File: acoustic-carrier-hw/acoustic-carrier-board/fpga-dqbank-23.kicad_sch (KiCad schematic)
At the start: 13 parts, among them IC1 ECP5-BGA256

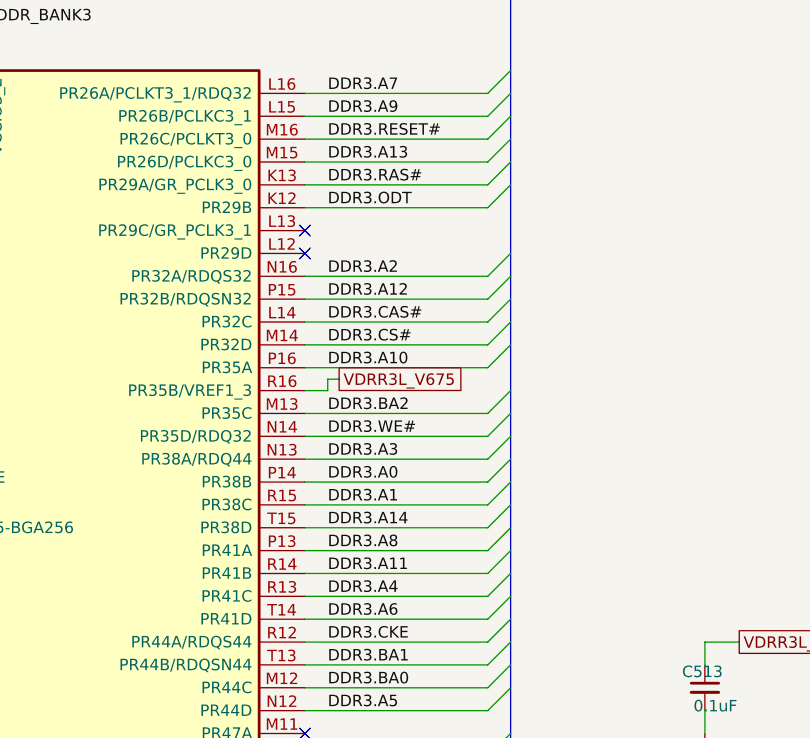
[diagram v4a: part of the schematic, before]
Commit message: [carrier] Progressing on ddr3 routing (next) check all ddr3 signals for errors, start length matching
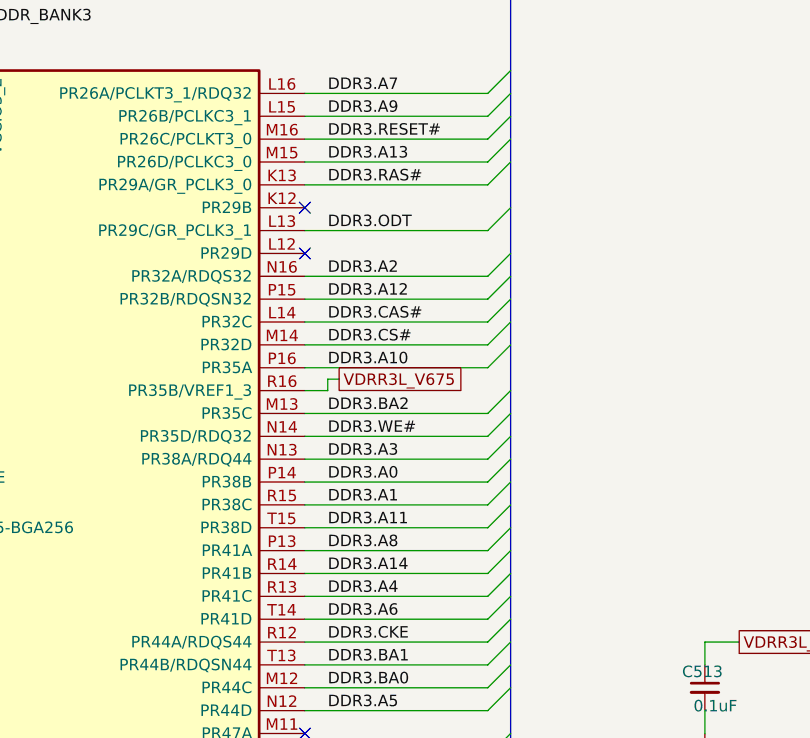
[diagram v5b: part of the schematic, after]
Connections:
- net DDR3.A11: now also IC1.T15 (PR38D); no longer IC1.R14 (PR41B)
- net DDR3.A14: now also IC1.R14 (PR41B); no longer IC1.T15 (PR38D)
- net DDR3.ODT: now also IC1.L13 (PR29C/GR_PCLK3_1); no longer IC1.K12 (PR29B)
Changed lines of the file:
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@@
+	)
+	(no_connect
+		(at 212.09 71.12)
 	)
 	(no_connect
@@
 		(at 71.12 92.71)
 	)
-	(no_connect
-		(at 212.09 73.66)
-	)
 	(bus_entry
 		(at 234.95 81.28)
@@
 	)
 	(bus_entry
+		(at 234.95 71.12)
+		(size -2.54 2.54)
+		(stroke
+			(width 0)
+			(type default)
+		)
+	)
+	(bus_entry
 		(at 234.95 63.5)
 		(size -2.54 2.54)
@@
 	)
 	(bus_entry
-		(at 234.95 68.58)
-		(size -2.54 2.54)
-		(stroke
-			(width 0)
-			(type default)
-		)
-	)
-	(bus_entry
 		(at 234.95 83.82)
 		(size -2.54 2.54)
@@
 	(bus
 		(pts
+			(xy 234.95 71.12) (xy 234.95 76.2)
+		)
+		(stroke
+			(width 0)
+			(type default)
+		)
+	)
+	(bus
+		(pts
 			(xy 104.14 125.73) (xy 104.14 113.03)
 		)
@@
 	(bus
 		(pts
-			(xy 234.95 66.04) (xy 234.95 68.58)
+			(xy 234.95 66.04) (xy 234.95 71.12)
 		)
 		(stroke
@@
 		)
 	)
-	(wire
-		(pts
-			(xy 212.09 71.12) (xy 232.41 71.12)
-		)
-		(stroke
-			(width 0)
-			(type default)
-		)
-	)
 	(bus
 		(pts
@@
 		)
 	)
-	(bus
-		(pts
-			(xy 234.95 68.58) (xy 234.95 76.2)
-		)
-		(stroke
-			(width 0)
-			(type default)
-		)
-	)
 	(wire
 		(pts
@@
 		(pts
 			(xy 71.12 125.73) (xy 101.6 125.73)
+		)
+		(stroke
+			(width 0)
+			(type default)
+		)
+	)
+	(wire
+		(pts
+			(xy 212.09 73.66) (xy 232.41 73.66)
 		)
 		(stroke
@@
 		)
 	)
+	(label "DDR3.A11"
+		(at 214.63 106.68 0)
+		(effects
+			(font
+				(size 1.27 1.27)
+			)
+			(justify left bottom)
+		)
+	)
 	(label "DDR3.A5"
 		(at 214.63 127 0)
@@
 		)
 	)
-	(label "DDR3.A11"
-		(at 214.63 111.76 0)
-		(effects
-			(font
-				(size 1.27 1.27)
-			)
-			(justify left bottom)
-		)
-	)
 	(label "DDR3.DQ9"
 		(at 88.9 69.85 180)
@@
 		)
 	)
-	(label "DDR3.A14"
-		(at 214.63 106.68 0)
-		(effects
-			(font
-				(size 1.27 1.27)
-			)
-			(justify left bottom)
-		)
-	)
 	(label "DDR3.CS#"
 		(at 214.63 86.36 0)
@@
 		)
 	)
+	(label "DDR3.A14"
+		(at 214.63 111.76 0)
+		(effects
+			(font
+				(size 1.27 1.27)
+			)
+			(justify left bottom)
+		)
+	)
 	(label "DDR3.CAS#"
 		(at 214.63 83.82 0)
@@
 		)
 	)
+	(label "DDR3.ODT"
+		(at 214.63 73.66 0)
+		(effects
+			(font
+				(size 1.27 1.27)
+			)
+			(justify left bottom)
+		)
+	)
 	(label "DDR3.DQ6"
 		(at 87.63 110.49 0)
 		(effects
 			(font
-				(size 1.27 1.27)
-			)
-			(justify left bottom)
-		)
-	)
-	(label "DDR3.ODT"
-		(at 214.63 71.12 0)
-		(effects
-			(font

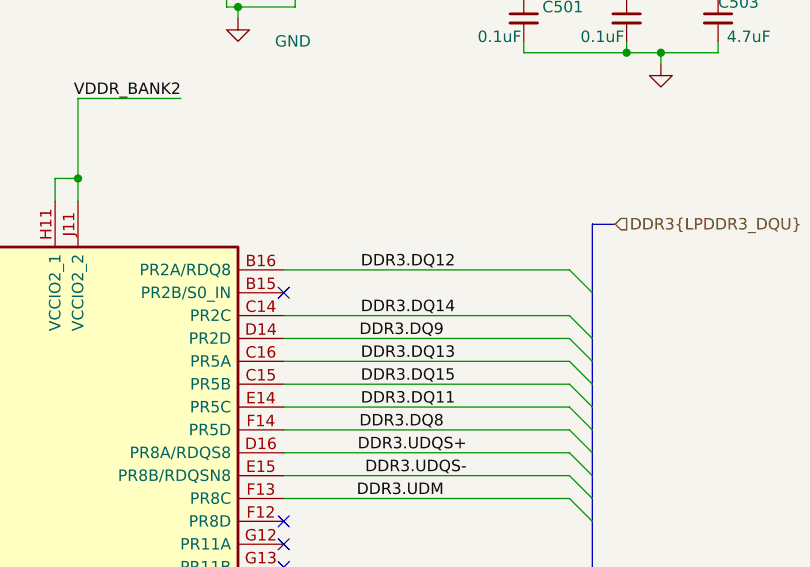
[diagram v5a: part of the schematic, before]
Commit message: [carrier] Changed all vias to (pcheaper) 0.2/0.35 size (next) create basic test-VHDL for clock-signal fanout checks
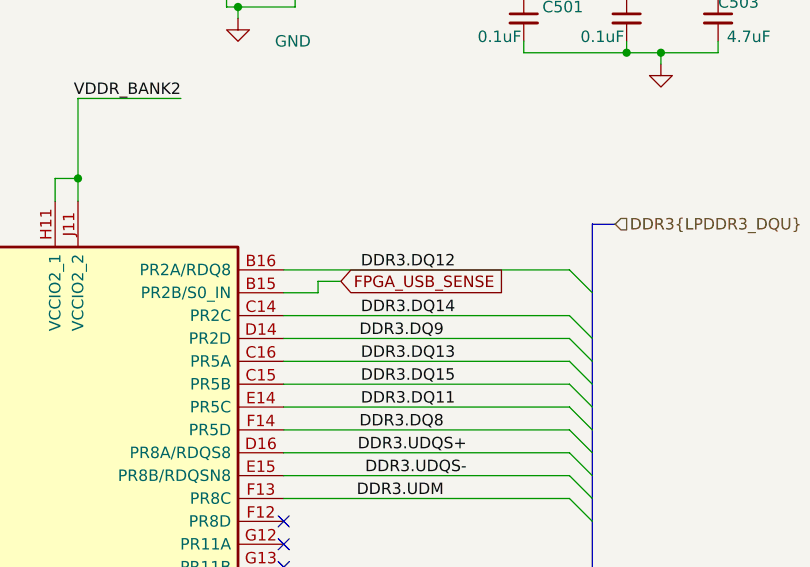
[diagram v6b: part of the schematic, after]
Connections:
- net FPGA_USB_SENSE: now reaches IC1.B15 (PR2B/S0_IN)
- no-connect marks 13 -> 12
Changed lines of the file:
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@@
-	)
-	(no_connect
-		(at 71.12 64.77)
 	)
 	(no_connect
@@
 	(wire
 		(pts
+			(xy 74.93 63.5) (xy 74.93 64.77)
+		)
+		(stroke
+			(width 0)
+			(type default)
+		)
+	)
+	(wire
+		(pts
 			(xy 245.11 36.83) (xy 245.11 38.1)
 		)
@@
 		)
 	)
+	(wire
+		(pts
+			(xy 74.93 64.77) (xy 71.12 64.77)
+		)
+		(stroke
+			(width 0)
+			(type default)
+		)
+	)
 	(bus
 		(pts
@@
 		(pts
 			(xy 71.12 138.43) (xy 101.6 138.43)
+		)
+		(stroke
+			(width 0)
+			(type default)
+		)
+	)
+	(wire
+		(pts
+			(xy 74.93 63.5) (xy 77.47 63.5)
 		)
 		(stroke
@@
 			(effects
 				(font
+					(size 1.27 1.27)
+				)
+				(justify left)
+				(hide yes)
+			)
+		)
+	)
+	(global_label "FPGA_USB_SENSE"
+		(shape input)
+		(at 77.47 63.5 0)
+		(fields_autoplaced yes)
+		(effects
+			(font
+				(size 1.27 1.27)
+			)
+			(justify left)
+		)
+		(property "Intersheetrefs" "${INTERSHEET_REFS}"
+			(at 96.9651 63.5 0)
+			(effects
+				(font

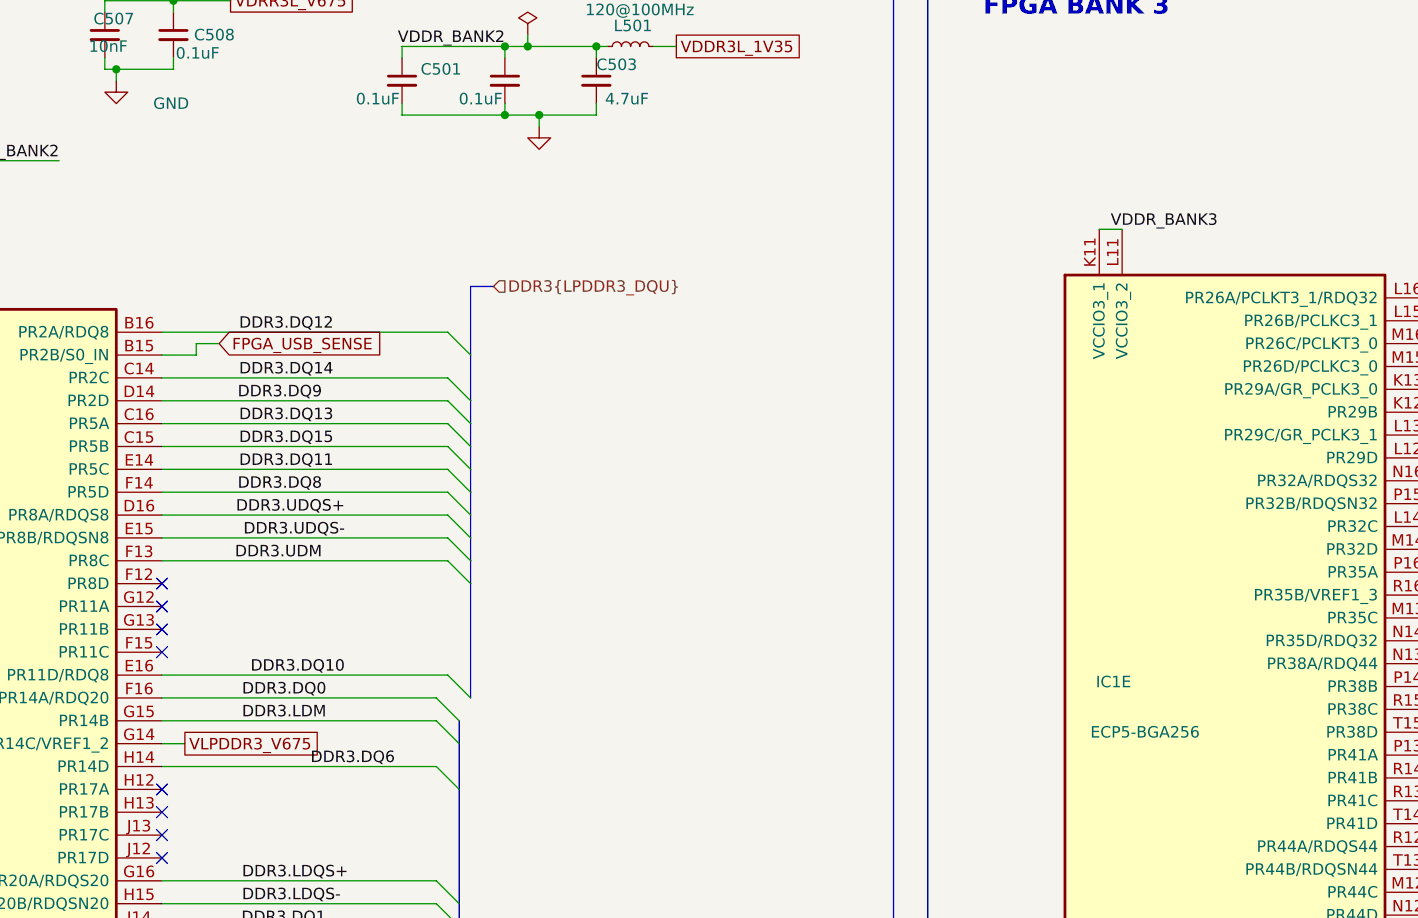
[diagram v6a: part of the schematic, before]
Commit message: [carrier] Started writing constraints file for ECP5U-FPGA (next) finish constraints file, try basic synthesis with pins and hello-world
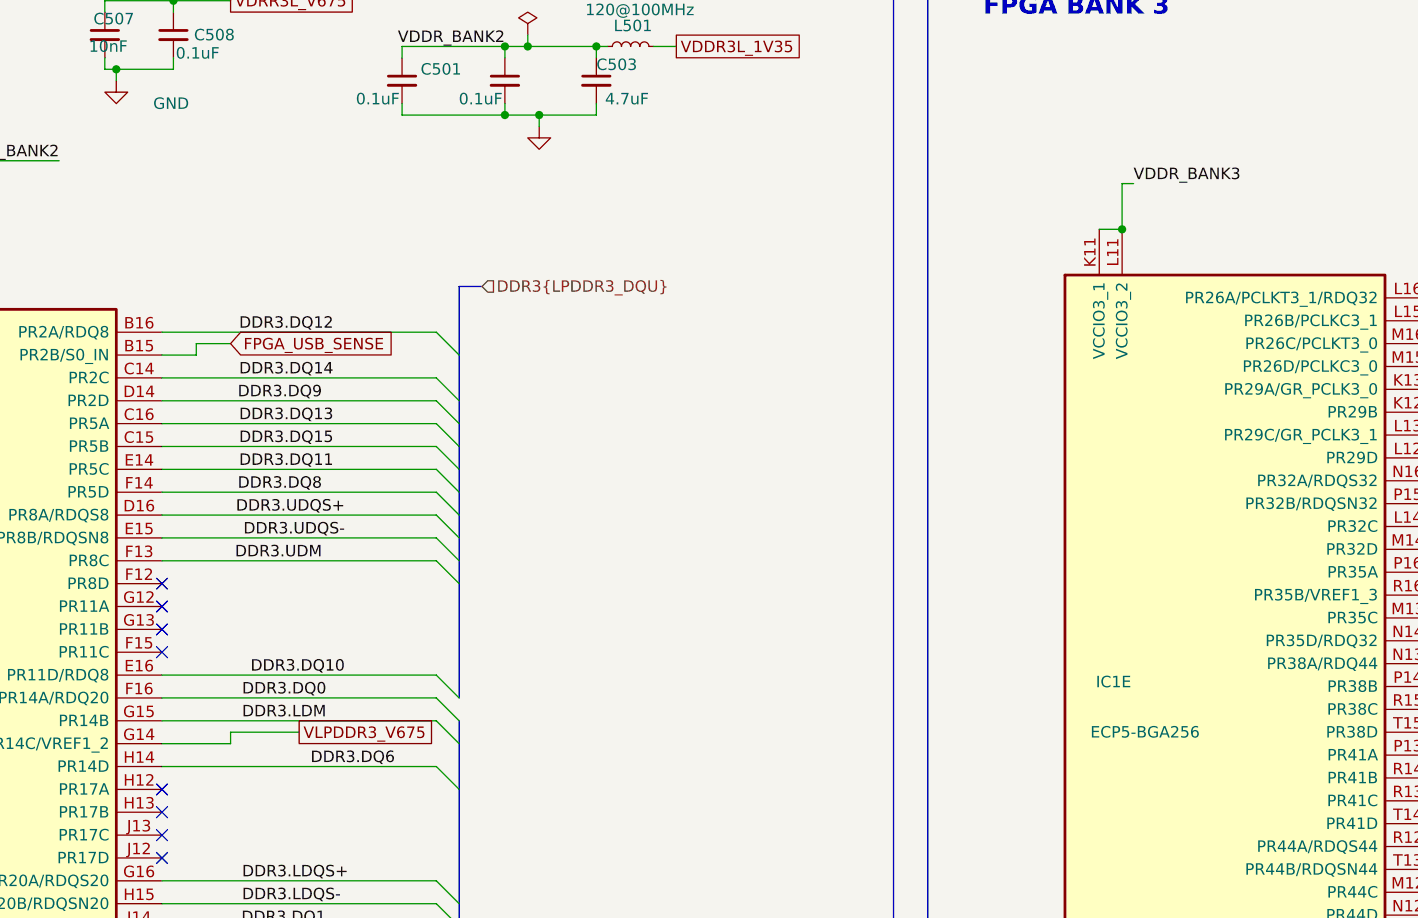
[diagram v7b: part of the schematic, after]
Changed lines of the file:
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@@
+	)
+	(junction
+		(at 177.8 50.8)
+		(diameter 0)
+		(color 0 0 0 0)
 	)
 	(junction
@@
 	)
 	(bus_entry
-		(at 105.41 90.17)
+		(at 104.14 90.17)
 		(size -2.54 -2.54)
 		(stroke
@@
 	)
 	(bus_entry
-		(at 102.87 72.39)
+		(at 101.6 72.39)
 		(size 2.54 2.54)
 		(stroke
@@
 	)
 	(bus_entry
-		(at 105.41 64.77)
+		(at 104.14 64.77)
 		(size -2.54 -2.54)
 		(stroke
@@
 	)
 	(bus_entry
-		(at 105.41 85.09)
+		(at 104.14 85.09)
 		(size -2.54 -2.54)
 		(stroke
@@
 	)
 	(bus_entry
-		(at 105.41 80.01)
+		(at 104.14 80.01)
 		(size -2.54 -2.54)
 		(stroke
@@
 	)
 	(bus_entry
-		(at 105.41 87.63)
+		(at 104.14 87.63)
 		(size -2.54 -2.54)
 		(stroke
@@
 	)
 	(bus_entry
-		(at 105.41 72.39)
+		(at 104.14 72.39)
 		(size -2.54 -2.54)
 		(stroke
@@
 	)
 	(bus_entry
-		(at 105.41 82.55)
+		(at 104.14 82.55)
 		(size -2.54 -2.54)
 		(stroke
@@
 	)
 	(bus_entry
-		(at 105.41 69.85)
+		(at 104.14 69.85)
 		(size -2.54 -2.54)
 		(stroke
@@
 	)
 	(bus_entry
-		(at 102.87 100.33)
+		(at 101.6 100.33)
 		(size 2.54 2.54)
 		(stroke
@@
 	)
 	(bus_entry
-		(at 105.41 77.47)
+		(at 104.14 77.47)
 		(size -2.54 -2.54)
 		(stroke
@@
 	(bus
 		(pts
-			(xy 105.41 85.09) (xy 105.41 82.55)
-		)
-		(stroke
-			(width 0)
-			(type default)
-		)
-	)
-	(wire
-		(pts
-			(xy 71.12 69.85) (xy 102.87 69.85)
+			(xy 104.14 85.09) (xy 104.14 82.55)
+		)
+		(stroke
+			(width 0)
+			(type default)
+		)
+	)
+	(wire
+		(pts
+			(xy 71.12 69.85) (xy 101.6 69.85)
 		)
 		(stroke
@@
 	(bus
 		(pts
-			(xy 105.41 57.15) (xy 107.95 57.15)
+			(xy 104.14 57.15) (xy 106.68 57.15)
 		)
 		(stroke
@@
 	(wire
 		(pts
+			(xy 78.74 106.68) (xy 78.74 107.95)
+		)
+		(stroke
+			(width 0)
+			(type default)
+		)
+	)
+	(wire
+		(pts
 			(xy 175.26 50.8) (xy 177.8 50.8)
 		)
@@
 	(bus
 		(pts
-			(xy 105.41 64.77) (xy 105.41 69.85)
+			(xy 104.14 64.77) (xy 104.14 69.85)
+		)
+		(stroke
+			(width 0)
+			(type default)
+		)
+	)
+	(wire
+		(pts
+			(xy 177.8 45.72) (xy 177.8 50.8)
 		)
 		(stroke
@@
 	(bus
 		(pts
-			(xy 105.41 77.47) (xy 105.41 74.93)
+			(xy 104.14 77.47) (xy 104.14 74.93)
 		)
 		(stroke
@@
 	(wire
 		(pts
-			(xy 71.12 77.47) (xy 102.87 77.47)
+			(xy 71.12 77.47) (xy 101.6 77.47)
 		)
 		(stroke
@@
 	(wire
 		(pts
-			(xy 71.12 87.63) (xy 102.87 87.63)
+			(xy 71.12 87.63) (xy 101.6 87.63)
 		)
 		(stroke
@@
 	(bus
 		(pts
-			(xy 105.41 69.85) (xy 105.41 72.39)
+			(xy 104.14 69.85) (xy 104.14 72.39)
 		)
 		(stroke
@@
 	(wire
 		(pts
-			(xy 71.12 72.39) (xy 102.87 72.39)
+			(xy 71.12 72.39) (xy 101.6 72.39)
 		)
 		(stroke
@@
 	(wire
 		(pts
-			(xy 71.12 85.09) (xy 102.87 85.09)
+			(xy 71.12 85.09) (xy 101.6 85.09)
+		)
+		(stroke
+			(width 0)
+			(type default)
+		)
+	)
+	(wire
+		(pts
+			(xy 179.07 45.72) (xy 177.8 45.72)
 		)
 		(stroke
@@
 	(wire
 		(pts
-			(xy 71.12 107.95) (xy 73.66 107.95)
+			(xy 78.74 106.68) (xy 86.36 106.68)
 		)
 		(stroke
@@
 	(bus
 		(pts
-			(xy 105.41 80.01) (xy 105.41 77.47)
+			(xy 104.14 80.01) (xy 104.14 77.47)
+		)
+		(stroke
+			(width 0)
+			(type default)
+		)
+	)
+	(wire
+		(pts
+			(xy 78.74 107.95) (xy 71.12 107.95)
 		)
 		(stroke
@@
 	(wire
 		(pts
-			(xy 71.12 62.23) (xy 102.87 62.23)
+			(xy 71.12 62.23) (xy 101.6 62.23)
 		)
 		(stroke
@@
 	(bus
 		(pts
-			(xy 105.41 90.17) (xy 105.41 102.87)
+			(xy 104.14 90.17) (xy 104.14 102.87)
 		)
 		(stroke
@@
 	(wire
 		(pts
-			(xy 71.12 80.01) (xy 102.87 80.01)
+			(xy 71.12 80.01) (xy 101.6 80.01)
 		)
 		(stroke
@@
 	(wire
 		(pts
-			(xy 71.12 82.55) (xy 102.87 82.55)
+			(xy 71.12 82.55) (xy 101.6 82.55)
 		)
 		(stroke
@@
 	(wire
 		(pts
-			(xy 71.12 100.33) (xy 102.87 100.33)
+			(xy 71.12 100.33) (xy 101.6 100.33)
 		)
 		(stroke
@@
 	(bus
 		(pts
-			(xy 105.41 72.39) (xy 105.41 74.93)
+			(xy 104.14 72.39) (xy 104.14 74.93)
 		)
 		(stroke
@@
 	(wire
 		(pts
-			(xy 71.12 74.93) (xy 102.87 74.93)
-		)
-		(stroke
-			(width 0)
-			(type default)
-		)
-	)
-	(bus
-		(pts
-			(xy 105.41 64.77) (xy 105.41 57.15)
+			(xy 71.12 74.93) (xy 101.6 74.93)
+		)
+		(stroke
+			(width 0)
+			(type default)
+		)
+	)
+	(bus
+		(pts
+			(xy 104.14 64.77) (xy 104.14 57.15)
 		)
 		(stroke
@@
 	(bus
 		(pts
-			(xy 105.41 82.55) (xy 105.41 80.01)
+			(xy 104.14 82.55) (xy 104.14 80.01)
 		)
 		(stroke
@@
 	(wire
 		(pts
-			(xy 71.12 67.31) (xy 102.87 67.31)
+			(xy 71.12 67.31) (xy 101.6 67.31)
 		)
 		(stroke
@@
 	(wire
 		(pts
-			(xy 74.93 63.5) (xy 77.47 63.5)
-		)
-		(stroke
-			(width 0)
-			(type default)
-		)
-	)
-	(bus
-		(pts
-			(xy 105.41 87.63) (xy 105.41 85.09)
+			(xy 74.93 63.5) (xy 78.74 63.5)
+		)
+		(stroke
+			(width 0)
+			(type default)
+		)
+	)
+	(bus
+		(pts
+			(xy 104.14 87.63) (xy 104.14 85.09)
 		)
 		(stroke
@@
 	(bus
 		(pts
-			(xy 105.41 90.17) (xy 105.41 87.63)
+			(xy 104.14 90.17) (xy 104.14 87.63)
 		)
 		(stroke
@@
 	)
 	(label "VDDR_BANK3"
-		(at 176.53 50.8 0)
+		(at 179.07 45.72 0)
 		(effects
 			(font
@@
 	(global_label "VLPDDR3_V675"
 		(shape passive)
-		(at 73.66 107.95 0)
+		(at 86.36 106.68 0)
 		(fields_autoplaced yes)
 		(effects
@@
 		)
 		(property "Intersheetrefs" "${INTERSHEET_REFS}"
-			(at 89.6248 107.95 0)
+			(at 102.3248 106.68 0)
 			(effects
 				(font
@@
 	(global_label "FPGA_USB_SENSE"
 		(shape input)
-		(at 77.47 63.5 0)
+		(at 78.74 63.5 0)
 		(fields_autoplaced yes)
 		(effects
@@
 		)
 		(property "Intersheetrefs" "${INTERSHEET_REFS}"
-			(at 96.9651 63.5 0)
+			(at 98.2351 63.5 0)
 			(effects
 				(font
@@
 	(hierarchical_label "DDR3{LPDDR3_DQU}"
 		(shape input)
-		(at 107.95 57.15 0)
-		(effects
-			(font
+		(at 106.68 57.15 0)
+		(effects
+			(font
